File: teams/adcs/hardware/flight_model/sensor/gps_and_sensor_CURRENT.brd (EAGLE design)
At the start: 94 x 94 mm, 56 parts, among them U1 LT1761-X, U2 LT1761-X, U3 OEM719, U4 LTC3624

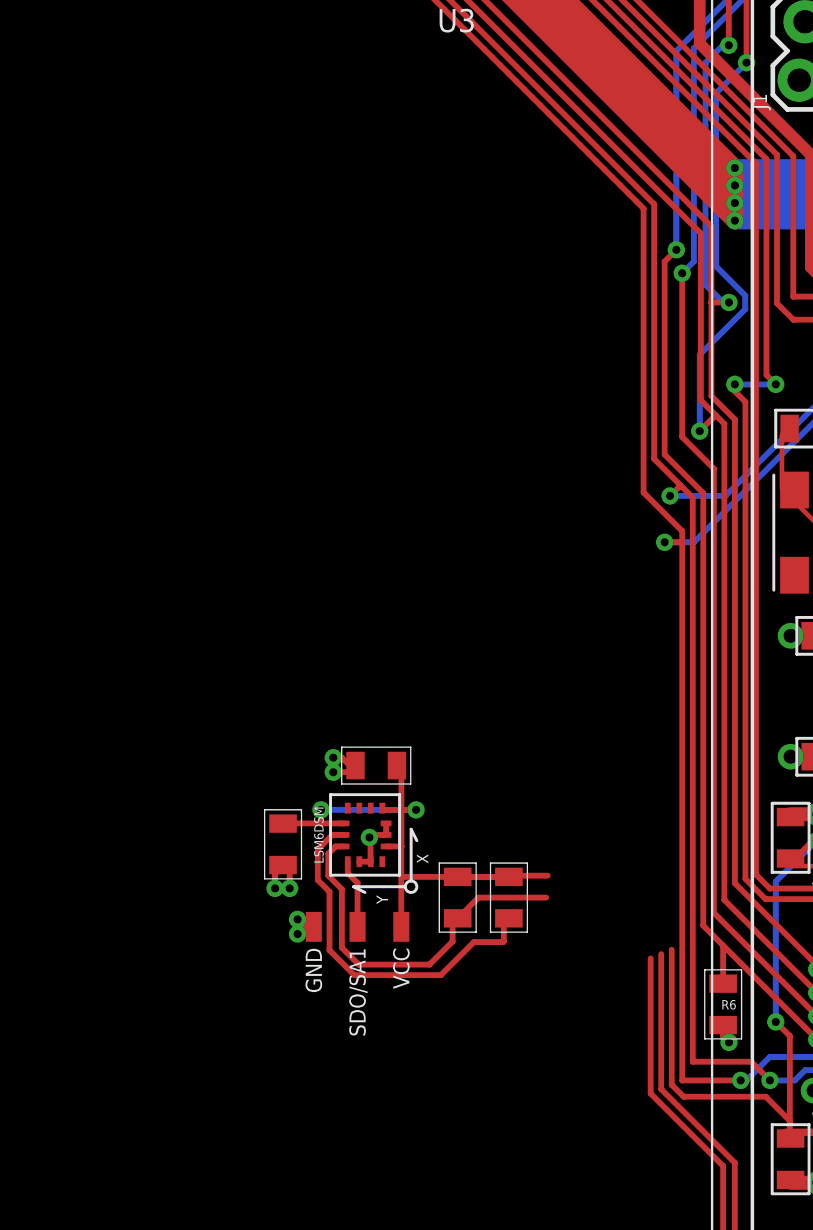
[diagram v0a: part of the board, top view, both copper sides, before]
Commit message: ADCS/Sensor: Add jumper connections to sensors
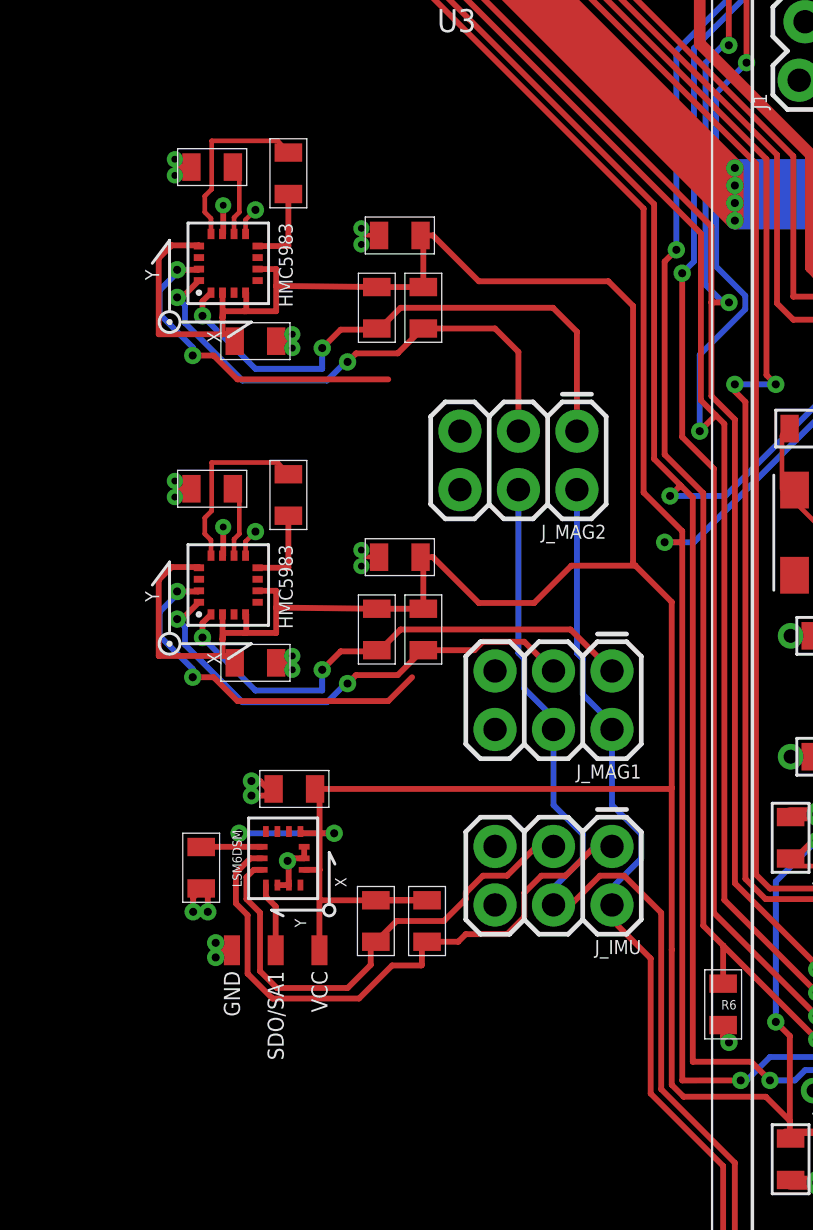
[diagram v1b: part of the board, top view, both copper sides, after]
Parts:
- added C29, C37: 4.7 uF, DubSat1 Components:0805
- added C30, C38: 0.22 uF, DubSat1 Components:0805
- added C31, C39: 0.1µF, DubSat1 Components:0805
- added C32, C40: 0.1 uF, DubSat1 Components:0805
- added J_IMU, J_MAG1, J_MAG2: (no value), SparkFun-Connectors:2X3
- added R11, R12, R15, R16: 10 k, DubSat1 Components:0805
- added U$6, U$8: HMC5983, DubSat1 Components:HMC5983
- moved U$5 3.70 mm to (42.1, 30.0)
- moved C25 3.70 mm to (38.5, 29.6)
- moved R10 3.70 mm to (48.4, 27.2)
- moved R9 3.70 mm to (46.1, 27.2)
- moved SDO/SA1 3.70 mm to (41.8, 26.0)
- moved C26 3.70 mm to (42.6, 33.0)
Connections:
- new net IMU_SCL: J_IMU.1, R10.2, U$5.SCL
- new net IMU_SDA: J_IMU.3, R9.2, U$5.SDA
- new net MA1G_C2: C29.1, U$6.C1
- new net MAG1_DRDY: U$6.DRDY
- new net MAG1_SCL: J_MAG1.1, R11.2, U$6.SCL/SPI_SCK
- new net MAG1_SDA: J_MAG1.3, R12.2, U$6.SDA/SPI_SDI
- new net MAG1_SETC1: C30.1, U$6.SETC
- new net MAG1_SETP1: C30.2, U$6.SETP
- new net MAG2_C1: C37.1, U$8.C1
- new net MAG2_DRDY: U$8.DRDY
- new net MAG2_SCL: J_MAG2.1, R15.2, U$8.SCL/SPI_SCK
- new net MAG2_SDA: J_MAG2.3, R16.2, U$8.SDA/SPI_SDI
- new net MAG2_SETC: C38.1, U$8.SETC
- new net MAG2_SETP: C38.2, U$8.SETP
- net GND: now also C29.2, C31.1, C32.1, C37.2, C39.1, C40.1, J_IMU.5, J_IMU.6, J_MAG1.5, J_MAG1.6, J_MAG2.5, J_MAG2.6, U$6.GND, U$6.SOC, U$8.GND, U$8.SOC
- net I2C_SCL: now also J_IMU.2, J_MAG1.2, J_MAG2.2; no longer R10.2, U$5.SCL
- net I2C_SDA: now also J_IMU.4, J_MAG1.4, J_MAG2.4; no longer R9.2, U$5.SDA
- net LDO_3V3: now also C31.2, C32.2, C39.2, C40.2, R11.1, R12.1, R15.1, R16.1, U$6.!SPI_CS, U$6.I2C/!SPI, U$6.VDD, U$6.VDDIO, U$8.!SPI_CS, U$8.I2C/!SPI, U$8.VDD, U$8.VDDIO
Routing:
- net LDO_3V3: track 256.5 -> 371.6 mm
- net IMU_SCL: track 0.00 -> 26.1 mm
- net MAG2_SCL: track 0.00 -> 24.8 mm, vias 0 -> 2
- net MAG2_SDA: track 0.00 -> 22.8 mm, vias 0 -> 2
- net MAG1_SCL: track 0.00 -> 22.3 mm, vias 0 -> 2
- net IMU_SDA: track 0.00 -> 21.6 mm
- net MAG1_SDA: track 0.00 -> 21.1 mm, vias 0 -> 2
- net MAG1_DRDY: track 0.00 -> 16.0 mm, vias 0 -> 2
- net MAG2_DRDY: track 0.00 -> 14.5 mm, vias 0 -> 2
- net GND: track 62.1 -> 76.0 mm, vias 77 -> 93
- net I2C_SDA: track 117.5 -> 128.6 mm
- net MAG2_SETC: track 0.00 -> 7.84 mm
- net MAG1_SETC1: track 0.00 -> 7.84 mm
- net I2C_SCL: track 125.5 -> 132.5 mm
- net MAG2_SETP: track 0.00 -> 3.59 mm
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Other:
- board text added: "HMC5983 1"
- board text added: "HMC5983 2"
- board text added: "IMU"
- board text added: "MAG1"
- board text added: "MAG2"
